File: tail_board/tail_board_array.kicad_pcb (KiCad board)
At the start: 2 copper layers, 83.8 x 91.1 mm, 80 parts, among them J1 Conn_01x05, J2 Conn_01x05

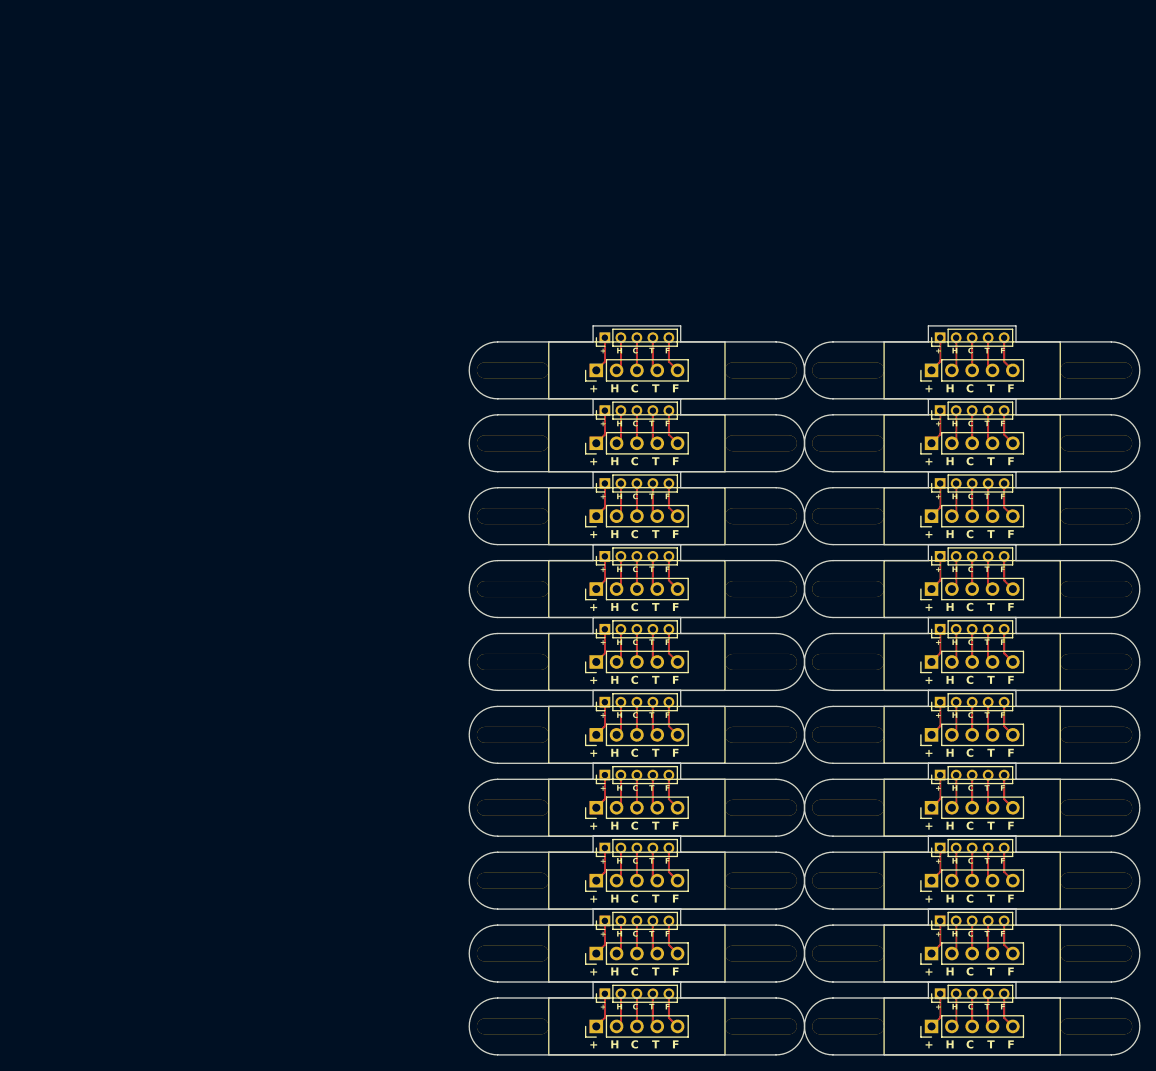
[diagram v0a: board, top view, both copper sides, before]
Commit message: feat: modify logo
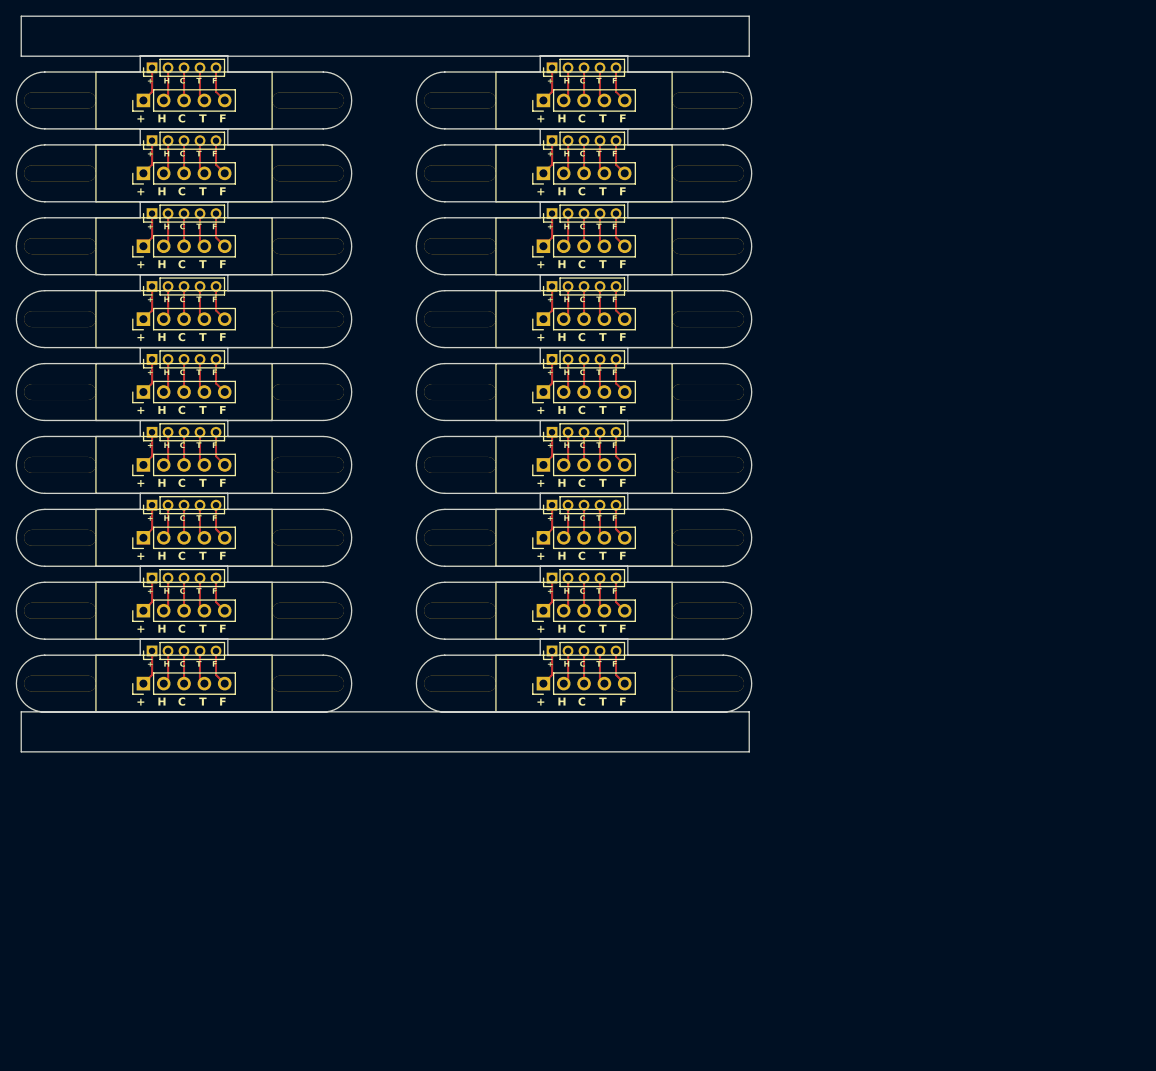
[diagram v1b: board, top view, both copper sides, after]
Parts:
- removed the J1 at (157.8, 138.2)
- removed the J1 at (115.9, 110.9)
- removed the J1 at (157.8, 92.7)
- removed the J1 at (115.9, 101.8)
- removed the J1 at (157.8, 101.8)
- removed the J1 at (115.9, 129.1)
- removed the J1 at (115.9, 165.6)
- removed the J1 at (115.9, 156.5)
- removed the J1 at (115.9, 147.3)
- removed the J1 at (157.8, 120.0)
- removed the J1 at (157.8, 83.6)
- removed the J1 at (115.9, 138.2)
- removed the J1 at (157.8, 147.3)
- removed the J1 at (115.9, 92.7)
- removed the J1 at (157.8, 129.1)
- removed the J1 at (115.9, 83.6)
- removed the J1 at (157.8, 110.9)
- removed the J1 at (157.8, 156.5)
- removed the J1 at (115.9, 120.0)
- removed the J1 at (157.8, 165.6)
- removed the J2 at (117.0, 88.6)
- removed the J2 at (117.0, 152.4)
- removed the J2 at (158.9, 79.5)
- removed the J2 at (158.9, 161.5)
- removed the J2 at (158.9, 115.9)
- removed the J2 at (158.9, 88.6)
- removed the J2 at (117.0, 79.5)
- removed the J2 at (117.0, 143.3)
- removed the J2 at (158.9, 152.4)
- removed the J2 at (158.9, 97.7)
- removed the J2 at (117.0, 161.5)
- removed the J2 at (117.0, 106.8)
- removed the J2 at (158.9, 125.0)
- removed the J2 at (117.0, 134.1)
- removed the J2 at (158.9, 143.3)
- removed the J2 at (117.0, 125.0)
- removed the J2 at (158.9, 134.1)
- removed the J2 at (117.0, 97.7)
- removed the J2 at (117.0, 115.9)
- removed the J2 at (158.9, 106.8)
- removed the REF** at (178.4, 165.6)
- removed the REF** at (147.4, 92.7)
- removed the REF** at (105.5, 83.6)
- removed the REF** at (105.5, 138.2)
- removed the REF** at (105.5, 92.7)
- removed the REF** at (147.4, 165.6)
- removed the REF** at (147.4, 138.2)
- removed the REF** at (147.4, 120.0)
- removed the REF** at (178.4, 138.2)
- removed the REF** at (147.4, 110.9)
- removed the REF** at (105.5, 120.0)
- removed the REF** at (178.4, 83.6)
- removed the REF** at (147.4, 83.6)
- removed the REF** at (178.4, 101.8)
- removed the REF** at (105.5, 110.9)
- removed the REF** at (147.4, 101.8)
- removed the REF** at (136.5, 120.0)
- removed the REF** at (178.4, 147.3)
- removed the REF** at (136.5, 83.6)
- removed the REF** at (105.5, 129.1)
- removed the REF** at (147.4, 147.3)
- removed the REF** at (136.5, 101.8)
- removed the REF** at (178.4, 120.0)
- removed the REF** at (178.4, 110.9)
- removed the REF** at (178.4, 92.7)
- removed the REF** at (178.4, 156.5)
- removed the REF** at (136.5, 156.5)
- removed the REF** at (147.4, 156.5)
- removed the REF** at (136.5, 92.7)
- removed the REF** at (105.5, 101.8)
- removed the REF** at (136.5, 147.3)
- removed the REF** at (136.5, 110.9)
- removed the REF** at (147.4, 129.1)
- removed the REF** at (136.5, 129.1)
- removed the REF** at (105.5, 156.5)
- removed the REF** at (136.5, 138.2)
- removed the REF** at (178.4, 129.1)
- removed the REF** at (105.5, 165.6)
- removed the REF** at (136.5, 165.6)
- removed the REF** at (105.5, 147.3)
- added J1: Conn_01x05, Connector_PinHeader_2.54mm:PinHeader_1x05_P2.54mm_Vertical, F.Cu at (59.3, 68.0)
- added J1: Conn_01x05, Connector_PinHeader_2.54mm:PinHeader_1x05_P2.54mm_Vertical, F.Cu at (109.3, 122.7)
- added J1: Conn_01x05, Connector_PinHeader_2.54mm:PinHeader_1x05_P2.54mm_Vertical, F.Cu at (109.3, 113.6)
- added J1: Conn_01x05, Connector_PinHeader_2.54mm:PinHeader_1x05_P2.54mm_Vertical, F.Cu at (109.3, 49.8)
- added J1: Conn_01x05, Connector_PinHeader_2.54mm:PinHeader_1x05_P2.54mm_Vertical, F.Cu at (59.3, 49.8)
- added J1: Conn_01x05, Connector_PinHeader_2.54mm:PinHeader_1x05_P2.54mm_Vertical, F.Cu at (59.3, 122.7)
- added J1: Conn_01x05, Connector_PinHeader_2.54mm:PinHeader_1x05_P2.54mm_Vertical, F.Cu at (109.3, 77.2)
- added J1: Conn_01x05, Connector_PinHeader_2.54mm:PinHeader_1x05_P2.54mm_Vertical, F.Cu at (59.3, 77.2)
- added J1: Conn_01x05, Connector_PinHeader_2.54mm:PinHeader_1x05_P2.54mm_Vertical, F.Cu at (109.3, 86.3)
- added J1: Conn_01x05, Connector_PinHeader_2.54mm:PinHeader_1x05_P2.54mm_Vertical, F.Cu at (59.3, 113.6)
- added J1: Conn_01x05, Connector_PinHeader_2.54mm:PinHeader_1x05_P2.54mm_Vertical, F.Cu at (59.3, 95.4)
- added J1: Conn_01x05, Connector_PinHeader_2.54mm:PinHeader_1x05_P2.54mm_Vertical, F.Cu at (59.3, 58.9)
- added J1: Conn_01x05, Connector_PinHeader_2.54mm:PinHeader_1x05_P2.54mm_Vertical, F.Cu at (109.3, 104.5)
- added J1: Conn_01x05, Connector_PinHeader_2.54mm:PinHeader_1x05_P2.54mm_Vertical, F.Cu at (59.3, 86.3)
- added J1: Conn_01x05, Connector_PinHeader_2.54mm:PinHeader_1x05_P2.54mm_Vertical, F.Cu at (109.3, 58.9)
- added J1: Conn_01x05, Connector_PinHeader_2.54mm:PinHeader_1x05_P2.54mm_Vertical, F.Cu at (109.3, 95.4)
- added J1: Conn_01x05, Connector_PinHeader_2.54mm:PinHeader_1x05_P2.54mm_Vertical, F.Cu at (59.3, 104.5)
- added J1: Conn_01x05, Connector_PinHeader_2.54mm:PinHeader_1x05_P2.54mm_Vertical, F.Cu at (109.3, 68.0)
- added J2: Conn_01x05, Connector_PinHeader_2.00mm:PinHeader_1x05_P2.00mm_Vertical, F.Cu at (60.3, 45.7)
- added J2: Conn_01x05, Connector_PinHeader_2.00mm:PinHeader_1x05_P2.00mm_Vertical, F.Cu at (60.3, 91.3)
- added J2: Conn_01x05, Connector_PinHeader_2.00mm:PinHeader_1x05_P2.00mm_Vertical, F.Cu at (60.3, 100.4)
- added J2: Conn_01x05, Connector_PinHeader_2.00mm:PinHeader_1x05_P2.00mm_Vertical, F.Cu at (60.3, 64.0)
- added J2: Conn_01x05, Connector_PinHeader_2.00mm:PinHeader_1x05_P2.00mm_Vertical, F.Cu at (110.3, 91.3)
- added J2: Conn_01x05, Connector_PinHeader_2.00mm:PinHeader_1x05_P2.00mm_Vertical, F.Cu at (110.3, 73.1)
- added J2: Conn_01x05, Connector_PinHeader_2.00mm:PinHeader_1x05_P2.00mm_Vertical, F.Cu at (110.3, 54.8)
- added J2: Conn_01x05, Connector_PinHeader_2.00mm:PinHeader_1x05_P2.00mm_Vertical, F.Cu at (110.3, 118.6)
- added J2: Conn_01x05, Connector_PinHeader_2.00mm:PinHeader_1x05_P2.00mm_Vertical, F.Cu at (60.3, 54.8)
- added J2: Conn_01x05, Connector_PinHeader_2.00mm:PinHeader_1x05_P2.00mm_Vertical, F.Cu at (110.3, 45.7)
- added J2: Conn_01x05, Connector_PinHeader_2.00mm:PinHeader_1x05_P2.00mm_Vertical, F.Cu at (60.3, 118.6)
- added J2: Conn_01x05, Connector_PinHeader_2.00mm:PinHeader_1x05_P2.00mm_Vertical, F.Cu at (110.3, 64.0)
- added J2: Conn_01x05, Connector_PinHeader_2.00mm:PinHeader_1x05_P2.00mm_Vertical, F.Cu at (110.3, 82.2)
- added J2: Conn_01x05, Connector_PinHeader_2.00mm:PinHeader_1x05_P2.00mm_Vertical, F.Cu at (60.3, 109.5)
- added J2: Conn_01x05, Connector_PinHeader_2.00mm:PinHeader_1x05_P2.00mm_Vertical, F.Cu at (60.3, 73.1)
- added J2: Conn_01x05, Connector_PinHeader_2.00mm:PinHeader_1x05_P2.00mm_Vertical, F.Cu at (60.3, 82.2)
- added J2: Conn_01x05, Connector_PinHeader_2.00mm:PinHeader_1x05_P2.00mm_Vertical, F.Cu at (110.3, 100.4)
- added J2: Conn_01x05, Connector_PinHeader_2.00mm:PinHeader_1x05_P2.00mm_Vertical, F.Cu at (110.3, 109.5)
- added REF**: SolderWirePad_1x01_SMD_1x2mm, Connector_Wire:SolderWirePad_1x01_SMD_1x2mm, F.Cu at (129.9, 122.7)
- added REF**: SolderWirePad_1x01_SMD_1x2mm, Connector_Wire:SolderWirePad_1x01_SMD_1x2mm, F.Cu at (129.9, 95.4)
- added REF**: SolderWirePad_1x01_SMD_1x2mm, Connector_Wire:SolderWirePad_1x01_SMD_1x2mm, F.Cu at (79.9, 122.7)
- added REF**: SolderWirePad_1x01_SMD_1x2mm, Connector_Wire:SolderWirePad_1x01_SMD_1x2mm, F.Cu at (48.8, 77.2)
- added REF**: SolderWirePad_1x01_SMD_1x2mm, Connector_Wire:SolderWirePad_1x01_SMD_1x2mm, F.Cu at (98.8, 104.5)
- added REF**: SolderWirePad_1x01_SMD_1x2mm, Connector_Wire:SolderWirePad_1x01_SMD_1x2mm, F.Cu at (48.8, 86.3)
- added REF**: SolderWirePad_1x01_SMD_1x2mm, Connector_Wire:SolderWirePad_1x01_SMD_1x2mm, F.Cu at (98.8, 77.2)
- added REF**: SolderWirePad_1x01_SMD_1x2mm, Connector_Wire:SolderWirePad_1x01_SMD_1x2mm, F.Cu at (48.8, 95.4)
- added REF**: SolderWirePad_1x01_SMD_1x2mm, Connector_Wire:SolderWirePad_1x01_SMD_1x2mm, F.Cu at (129.9, 68.0)
- added REF**: SolderWirePad_1x01_SMD_1x2mm, Connector_Wire:SolderWirePad_1x01_SMD_1x2mm, F.Cu at (98.8, 68.0)
- added REF**: SolderWirePad_1x01_SMD_1x2mm, Connector_Wire:SolderWirePad_1x01_SMD_1x2mm, F.Cu at (98.8, 58.9)
- added REF**: SolderWirePad_1x01_SMD_1x2mm, Connector_Wire:SolderWirePad_1x01_SMD_1x2mm, F.Cu at (79.9, 68.0)
- added REF**: SolderWirePad_1x01_SMD_1x2mm, Connector_Wire:SolderWirePad_1x01_SMD_1x2mm, F.Cu at (98.8, 122.7)
- added REF**: SolderWirePad_1x01_SMD_1x2mm, Connector_Wire:SolderWirePad_1x01_SMD_1x2mm, F.Cu at (48.8, 104.5)
- added REF**: SolderWirePad_1x01_SMD_1x2mm, Connector_Wire:SolderWirePad_1x01_SMD_1x2mm, F.Cu at (79.9, 104.5)
- added REF**: SolderWirePad_1x01_SMD_1x2mm, Connector_Wire:SolderWirePad_1x01_SMD_1x2mm, F.Cu at (79.9, 86.3)
- added REF**: SolderWirePad_1x01_SMD_1x2mm, Connector_Wire:SolderWirePad_1x01_SMD_1x2mm, F.Cu at (98.8, 95.4)
- added REF**: SolderWirePad_1x01_SMD_1x2mm, Connector_Wire:SolderWirePad_1x01_SMD_1x2mm, F.Cu at (98.8, 113.6)
- added REF**: SolderWirePad_1x01_SMD_1x2mm, Connector_Wire:SolderWirePad_1x01_SMD_1x2mm, F.Cu at (79.9, 49.8)
- added REF**: SolderWirePad_1x01_SMD_1x2mm, Connector_Wire:SolderWirePad_1x01_SMD_1x2mm, F.Cu at (98.8, 86.3)
- added REF**: SolderWirePad_1x01_SMD_1x2mm, Connector_Wire:SolderWirePad_1x01_SMD_1x2mm, F.Cu at (129.9, 77.2)
- added REF**: SolderWirePad_1x01_SMD_1x2mm, Connector_Wire:SolderWirePad_1x01_SMD_1x2mm, F.Cu at (129.9, 86.3)
- added REF**: SolderWirePad_1x01_SMD_1x2mm, Connector_Wire:SolderWirePad_1x01_SMD_1x2mm, F.Cu at (129.9, 58.9)
- added REF**: SolderWirePad_1x01_SMD_1x2mm, Connector_Wire:SolderWirePad_1x01_SMD_1x2mm, F.Cu at (79.9, 113.6)
- added REF**: SolderWirePad_1x01_SMD_1x2mm, Connector_Wire:SolderWirePad_1x01_SMD_1x2mm, F.Cu at (48.8, 68.0)
- added REF**: SolderWirePad_1x01_SMD_1x2mm, Connector_Wire:SolderWirePad_1x01_SMD_1x2mm, F.Cu at (129.9, 113.6)
- added REF**: SolderWirePad_1x01_SMD_1x2mm, Connector_Wire:SolderWirePad_1x01_SMD_1x2mm, F.Cu at (48.8, 113.6)
- added REF**: SolderWirePad_1x01_SMD_1x2mm, Connector_Wire:SolderWirePad_1x01_SMD_1x2mm, F.Cu at (48.8, 49.8)
- added REF**: SolderWirePad_1x01_SMD_1x2mm, Connector_Wire:SolderWirePad_1x01_SMD_1x2mm, F.Cu at (79.9, 58.9)
- added REF**: SolderWirePad_1x01_SMD_1x2mm, Connector_Wire:SolderWirePad_1x01_SMD_1x2mm, F.Cu at (48.8, 122.7)
- added REF**: SolderWirePad_1x01_SMD_1x2mm, Connector_Wire:SolderWirePad_1x01_SMD_1x2mm, F.Cu at (98.8, 49.8)
- added REF**: SolderWirePad_1x01_SMD_1x2mm, Connector_Wire:SolderWirePad_1x01_SMD_1x2mm, F.Cu at (48.8, 58.9)
- added REF**: SolderWirePad_1x01_SMD_1x2mm, Connector_Wire:SolderWirePad_1x01_SMD_1x2mm, F.Cu at (79.9, 95.4)
- added REF**: SolderWirePad_1x01_SMD_1x2mm, Connector_Wire:SolderWirePad_1x01_SMD_1x2mm, F.Cu at (79.9, 77.2)
- added REF**: SolderWirePad_1x01_SMD_1x2mm, Connector_Wire:SolderWirePad_1x01_SMD_1x2mm, F.Cu at (129.9, 49.8)
- added REF**: SolderWirePad_1x01_SMD_1x2mm, Connector_Wire:SolderWirePad_1x01_SMD_1x2mm, F.Cu at (129.9, 104.5)
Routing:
- net +3.3V: track 90.8 -> 81.7 mm
- net /F: track 90.6 -> 81.5 mm
- net /T: track 86.4 -> 77.7 mm
- net GND: track 86.3 -> 77.7 mm
- net /S: track 81.7 -> 73.5 mm
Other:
- board size 83.8 x 91.1 mm -> 91.9 x 92 mm
